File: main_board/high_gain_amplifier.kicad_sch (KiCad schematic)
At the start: 0 parts

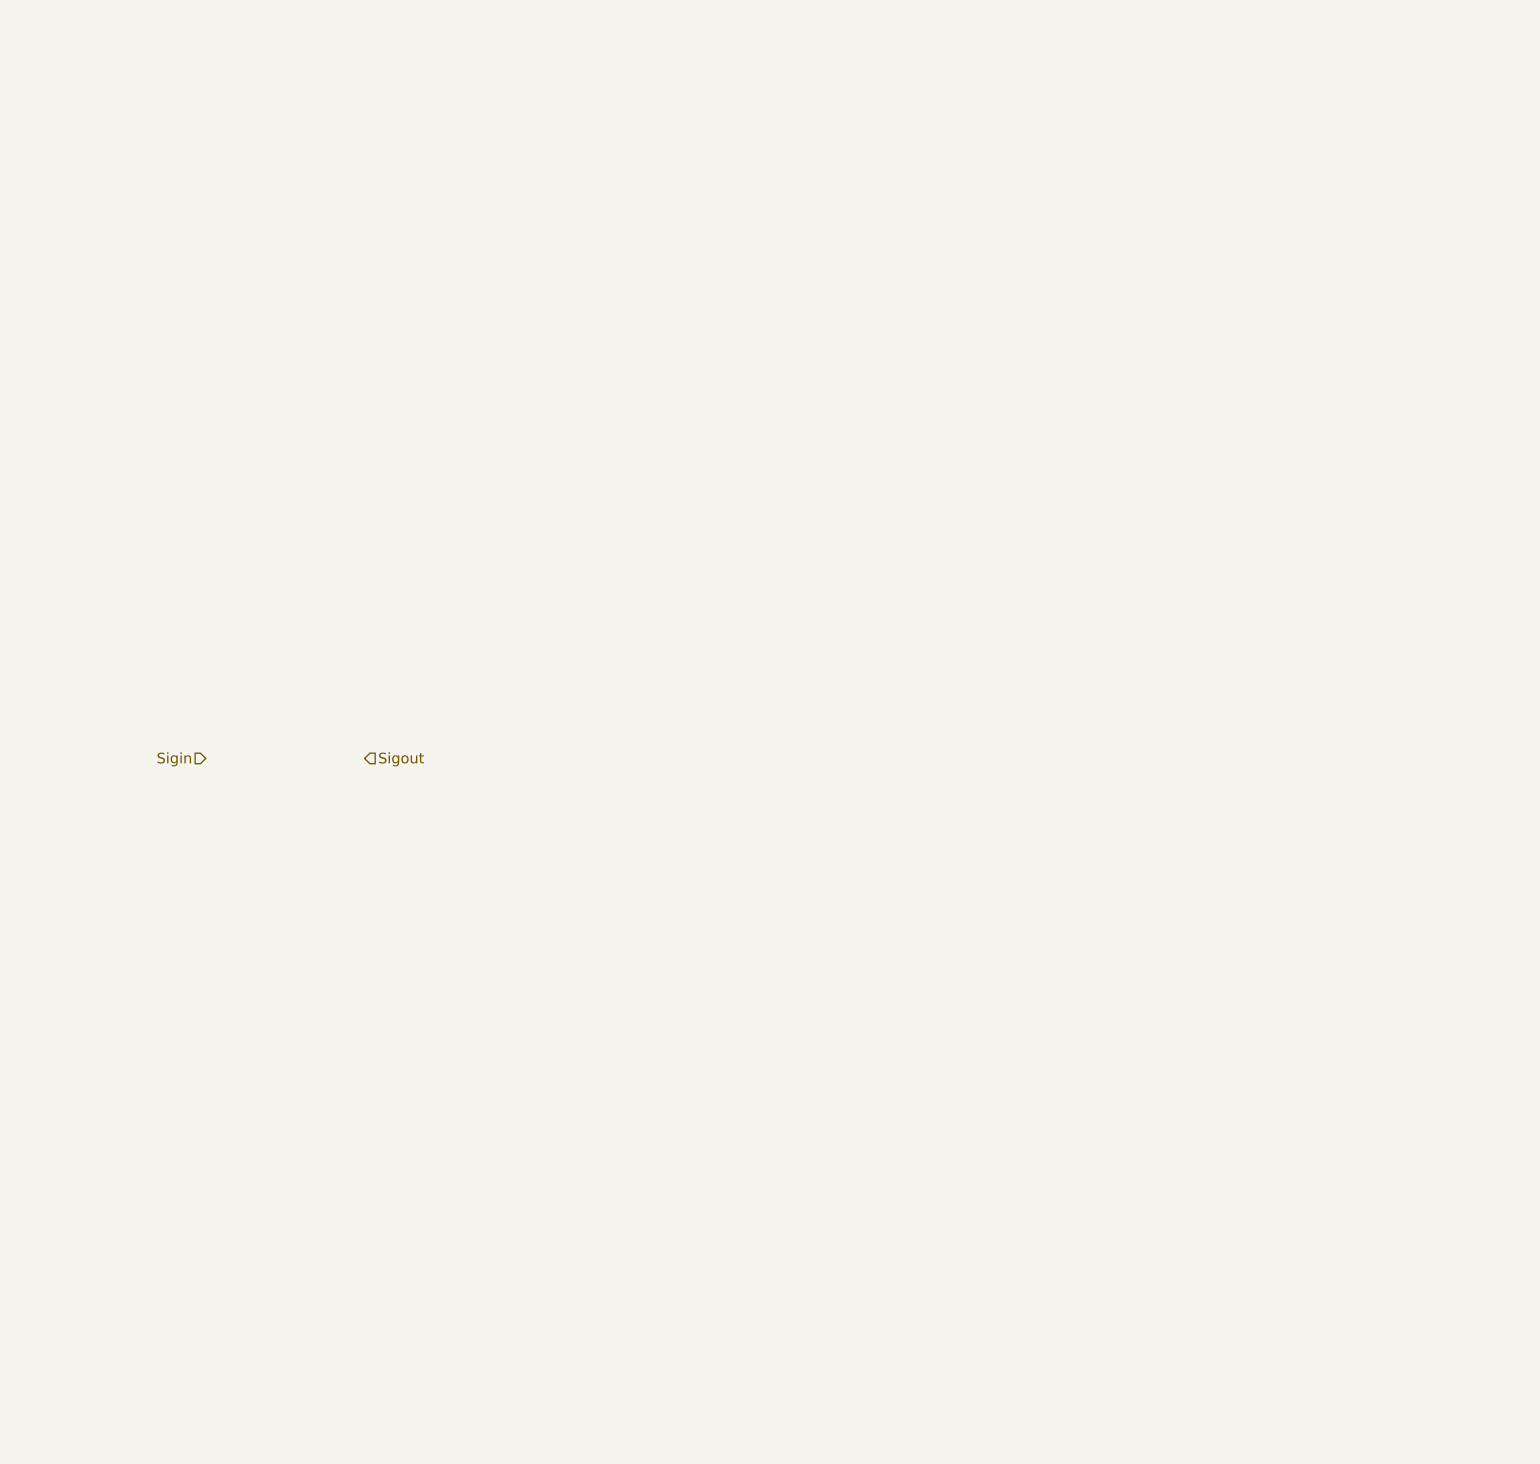
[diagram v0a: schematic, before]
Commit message: add schematic for high gain amplifier
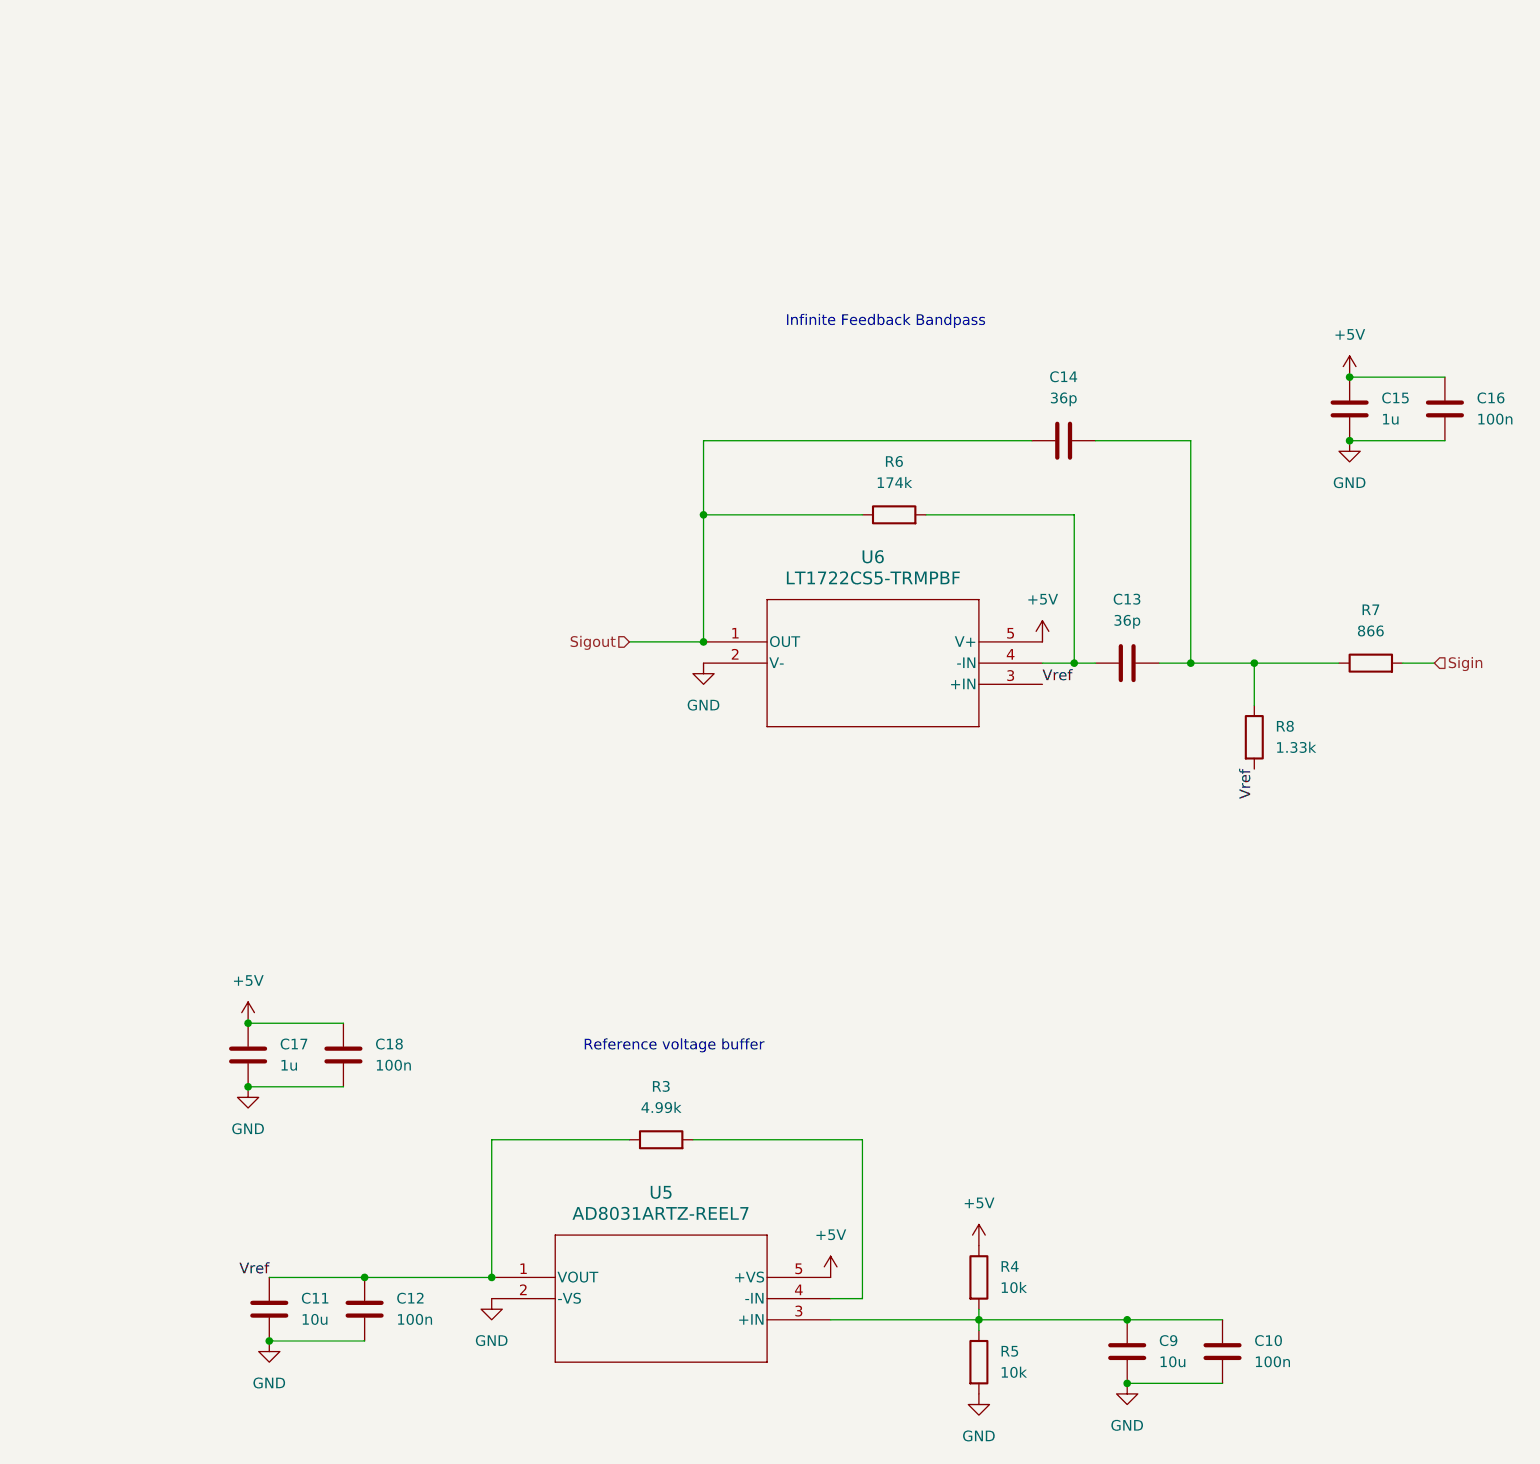
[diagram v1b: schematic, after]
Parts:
- added C10, C12, C16, C18: 100n, symbol Device:C
- added C11, C9: 10u, symbol Device:C
- added C13, C14: 36p, symbol Device:C
- added C15, C17: 1u, symbol Device:C
- added R3: 4.99k, symbol Device:R
- added R4, R5: 10k, symbol Device:R
- added R6: 174k, symbol Device:R
- added R7: 866, symbol Device:R
- added R8: 1.33k, symbol Device:R
- added U5: AD8031ARTZ-REEL7, RJ_5_ADI, symbol AD8031:AD8031ARTZ-REEL7
- added U6: LT1722CS5-TRMPBF, S_5_ADI, symbol LT172x:LT1722CS5-TRMPBF
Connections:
- net Sigin: now also R7.2
- net Sigout: now also C14.1, R6.1, U6.1 (OUT)
- new net: C10.1, C9.1, R4.2, R5.1, U5.3 (+IN)
- new net: C13.2, C14.2, R7.1, R8.1
- new net: R3.2, U5.4 (-IN)
- new net: C13.1, R6.2, U6.4 (-IN)
- new net +5V: C15.1, C16.1, C17.1, C18.1, R4.1, U5.5 (+VS), U6.5 (V+)
- new net GND: C10.2, C11.2, C12.2, C15.2, C16.2, C17.2, C18.2, C9.2, R5.2, U5.2 (-VS), U6.2 (V-)
- new net Vref: C11.1, C12.1, R3.1, R8.2, U5.1 (VOUT), U6.3 (+IN)
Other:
- note added: "Infinite Feedback Bandpass"
- note added: "Reference voltage buffer"

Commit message: update power supply decoupling caps
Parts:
- removed C15: 1u, symbol Device:C
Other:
- note added: "One bulk cap, one 100n for each IC"
- moved on the sheet: C16, C17, C18

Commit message: Added PCBway drc ruleset, connected mux IO, ADC SPI interface, Pot SPI interface & 0603 footprints to all passive devices.
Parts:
- C10, C11, C12, C13, C14, C16, C17, C18, C9: footprint (none) -> Capacitor_SMD:C_0603_1608Metric
- R3, R4, R5, R6, R7, R8: footprint (none) -> Resistor_SMD:R_0603_1608Metric
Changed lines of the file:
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@@
 			)
 		)
-		(property "Footprint" ""
+		(property "Footprint" "Resistor_SMD:R_0603_1608Metric"
 			(at 134.112 179.07 90)
 			(effects
@@
 			)
 		)
-		(property "Footprint" ""
+		(property "Footprint" "Capacitor_SMD:C_0603_1608Metric"
 			(at 39.0652 31.75 0)
 			(effects
@@
 			)
 		)
-		(property "Footprint" ""
+		(property "Footprint" "Capacitor_SMD:C_0603_1608Metric"
 			(at 166.0652 181.61 0)
 			(effects
@@
 			)
 		)
-		(property "Footprint" ""
+		(property "Footprint" "Capacitor_SMD:C_0603_1608Metric"
 			(at 51.7652 31.75 0)
 			(effects
@@
 			)
 		)
-		(property "Footprint" ""
+		(property "Footprint" "Resistor_SMD:R_0603_1608Metric"
 			(at 167.132 104.14 90)
 			(effects
@@
 			)
 		)
-		(property "Footprint" ""
+		(property "Footprint" "Capacitor_SMD:C_0603_1608Metric"
 			(at 27.6352 31.75 0)
 			(effects
@@
 			)
 		)
-		(property "Footprint" ""
+		(property "Footprint" "Capacitor_SMD:C_0603_1608Metric"
 			(at 149.86 67.6148 0)
 			(effects
@@
 			)
 		)
-		(property "Footprint" ""
+		(property "Footprint" "Capacitor_SMD:C_0603_1608Metric"
 			(at 154.6352 181.61 0)
 			(effects
@@
 			)
 		)
-		(property "Footprint" ""
+		(property "Footprint" "Resistor_SMD:R_0603_1608Metric"
 			(at 134.112 168.91 90)
 			(effects
@@
 			)
 		)
-		(property "Footprint" ""
+		(property "Footprint" "Capacitor_SMD:C_0603_1608Metric"
 			(at 157.48 94.2848 0)
 			(effects
@@
 			)
 		)
-		(property "Footprint" ""
+		(property "Footprint" "Resistor_SMD:R_0603_1608Metric"
 			(at 125.73 79.248 90)
 			(effects
@@
 			)
 		)
-		(property "Footprint" ""
+		(property "Footprint" "Capacitor_SMD:C_0603_1608Metric"
 			(at 51.7652 176.53 0)
 			(effects
@@
 			)
 		)
-		(property "Footprint" ""
+		(property "Footprint" "Resistor_SMD:R_0603_1608Metric"
 			(at 182.88 97.028 90)
 			(effects
@@
 			)
 		)
-		(property "Footprint" ""
+		(property "Footprint" "Resistor_SMD:R_0603_1608Metric"
 			(at 97.79 154.178 90)
 			(effects
@@
 			)
 		)
-		(property "Footprint" ""
+		(property "Footprint" "Capacitor_SMD:C_0603_1608Metric"
 			(at 63.1952 176.53 0)
 			(effects

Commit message: fix schematic parity warnings by providing full path to footprint
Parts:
- U5: footprint RJ_5_ADI -> AD8031:RJ_5_ADI
- U6: footprint S_5_ADI -> LT172x:S_5_ADI
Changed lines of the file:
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@@
 			)
 		)
-		(property "Footprint" "RJ_5_ADI"
+		(property "Footprint" "AD8031:RJ_5_ADI"
 			(at 95.25 176.53 0)
 			(effects
@@
 			)
 		)
-		(property "Footprint" "S_5_ADI"
+		(property "Footprint" "LT172x:S_5_ADI"
 			(at 123.825 101.6 0)
 			(effects
